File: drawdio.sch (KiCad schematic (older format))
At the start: 12 parts, among them P1 CONN_2, Q1 BC558, Q2 BC547, U1 LM555N

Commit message: Heavy work
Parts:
- removed P1: CONN_2, Pin_Headers:Pin_Header_Straight_1x02, symbol CONN_2
- removed P?: CONN_01X01, symbol CONN_01X01
- added P1: CONN_01X01, drawdio:Drawdio conn, symbol CONN_01X01
- added P2: CONN_01X02, drawdio:RS_mini_speaker_724-3100, symbol CONN_01X02
- added P3: CONN_01X01, drawdio:Drawdio_conn, symbol CONN_01X01
- added Q3: BC558, Housings_TO-92:TO-92_Molded_Wide_Oval, symbol BC558
- added Q4: BC547, Housings_TO-92:TO-92_Molded_Wide_Oval, symbol BC547
- BT1: footprint Pin_Headers:Pin_Header_Straight_1x02 -> drawdio:CR2025_Keystone_3002_button_cell_holder_SMT
- Q1, Q2: footprint drawdio:TO-92_JorFru_compact -> Housings_TO-92:TO-92_Molded_Wide_Oval
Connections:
- net GND: now also Q4.3 (E)
- net VCC: now also Q1.3 (E), Q3.3 (E); no longer Q1.1 (C)
- net at Q1.2 (B), Q2.2 (B): now also P2.2 (P2), Q3.1 (C), Q4.1 (C); no longer U1.3 (Q)
- net at R2.1, U1.7 (DIS): now also P3.1 (P1)
- net at R1.1: now also P1.1 (P1)
- net at C4.1, Q2.1 (C): now also Q1.1 (C); no longer Q1.3 (E)
- net at C4.2: now also P2.1 (P1)
- new net: Q3.2 (B), Q4.2 (B), U1.3 (Q)
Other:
- moved on the sheet: C4, Q1, Q2
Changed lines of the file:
@@
 LIBS:memory
 LIBS:xilinx
-LIBS:special
 LIBS:microcontrollers
 LIBS:dsp
@@
 $EndComp
 $Comp
-L CONN_2 P1
-U 1 1 5535819F
-P 5350 2000
-F 0 "P1" V 5300 2000 40  0000 C CNN
-F 1 "CONN_2" V 5400 2000 40  0000 C CNN
-F 2 "Pin_Headers:Pin_Header_Straight_1x02" H 5350 2000 60  0001 C CNN
-F 3 "" H 5350 2000 60  0000 C CNN
-	1    5350 2000
-	0    -1   -1   0
-$EndComp
-$Comp
 L R-RESCUE-drawdio R1
 U 1 1 55358209
@@
 L GND-RESCUE-drawdio #PWR01
 U 1 1 5535831F
-P 7400 4600
-F 0 "#PWR01" H 7400 4600 30  0001 C CNN
-F 1 "GND" H 7400 4530 30  0001 C CNN
-F 2 "" H 7400 4600 60  0000 C CNN
-F 3 "" H 7400 4600 60  0000 C CNN
-	1    7400 4600
+P 7950 4600
+F 0 "#PWR01" H 7950 4600 30  0001 C CNN
+F 1 "GND" H 7950 4530 30  0001 C CNN
+F 2 "" H 7950 4600 60  0000 C CNN
+F 3 "" H 7950 4600 60  0000 C CNN
+	1    7950 4600
 	1    0    0    -1
 $EndComp
@@
 $EndComp
 $Comp
-L BC547 Q2
-U 1 1 553583A7
-P 7300 4250
-F 0 "Q2" H 7300 4101 40  0000 R CNN
-F 1 "BC547" H 7300 4400 40  0000 R CNN
-F 2 "drawdio:TO-92_JorFru_compact" H 7200 4352 29  0000 C CNN
-F 3 "" H 7300 4250 60  0000 C CNN
-	1    7300 4250
-	1    0    0    -1
-$EndComp
-$Comp
 L BC558 Q1
 U 1 1 553583B6
-P 7300 3750
-F 0 "Q1" H 7300 3601 40  0000 R CNN
-F 1 "BC558" H 7300 3900 40  0000 R CNN
-F 2 "drawdio:TO-92_JorFru_compact" H 7200 3852 29  0000 C CNN
-F 3 "" H 7300 3750 60  0000 C CNN
-	1    7300 3750
-	1    0    0    -1
+P 7850 3750
+F 0 "Q1" H 7850 3601 40  0000 R CNN
+F 1 "BC558" H 7850 3900 40  0000 R CNN
+F 2 "Housings_TO-92:TO-92_Molded_Wide_Oval" H 7750 3852 29  0000 C CNN
+F 3 "" H 7850 3750 60  0000 C CNN
+	1    7850 3750
+	1    0    0    1
 $EndComp
 $Comp
 L CP-RESCUE-drawdio C4
 U 1 1 55358485
-P 7700 4000
-F 0 "C4" H 7750 4100 40  0000 L CNN
-F 1 "CP" H 7750 3900 40  0000 L CNN
-F 2 "Capacitors_Elko_ThroughHole:Elko_vert_11.2x6.3mm_RM2.5" H 7800 3850 30  0000 C CNN
-F 3 "~" H 7700 4000 300 0000 C CNN
-	1    7700 4000
-	0    -1   -1   0
+P 8450 4200
+F 0 "C4" H 8500 4300 40  0000 L CNN
+F 1 "CP" H 8500 4100 40  0000 L CNN
+F 2 "Capacitors_Elko_ThroughHole:Elko_vert_11.2x6.3mm_RM2.5" H 8550 4050 30  0000 C CNN
+F 3 "~" H 8450 4200 300 0000 C CNN
+	1    8450 4200
+	1    0    0    -1
 $EndComp
 $Comp
@@
 $EndComp
 $Comp
-L GND-RESCUE-drawdio #PWR06
+L GND-RESCUE-drawdio #PWR05
 U 1 1 553585E1
 P 3650 5050
-F 0 "#PWR06" H 3650 5050 30  0001 C CNN
+F 0 "#PWR05" H 3650 5050 30  0001 C CNN
 F 1 "GND" H 3650 4980 30  0001 C CNN
 F 2 "" H 3650 5050 60  0000 C CNN
@@
 $EndComp
 $Comp
-L VCC #PWR07
+L VCC #PWR06
 U 1 1 553585F0
-P 7400 3550
-F 0 "#PWR07" H 7400 3650 30  0001 C CNN
-F 1 "VCC" H 7400 3650 30  0000 C CNN
-F 2 "" H 7400 3550 60  0000 C CNN
-F 3 "" H 7400 3550 60  0000 C CNN
-	1    7400 3550
+P 7950 3550
+F 0 "#PWR06" H 7950 3650 30  0001 C CNN
+F 1 "VCC" H 7950 3650 30  0000 C CNN
+F 2 "" H 7950 3550 60  0000 C CNN
+F 3 "" H 7950 3550 60  0000 C CNN
+	1    7950 3550
 	1    0    0    -1
 $EndComp
@@
 F 0 "BT1" H 3250 4800 50  0000 C CNN
 F 1 "BATTERY" H 3250 4410 50  0000 C CNN
-F 2 "Pin_Headers:Pin_Header_Straight_1x02" H 3250 4600 60  0000 C CNN
+F 2 "drawdio:CR2025_Keystone_3002_button_cell_holder_SMT" H 3250 4600 60  0000 C CNN
 F 3 "~" H 3250 4600 60  0000 C CNN
 	1    3250 4600
@@
 $EndComp
 $Comp
-L GND-RESCUE-drawdio #PWR08
+L GND-RESCUE-drawdio #PWR07
 U 1 1 558086F5
 P 4600 4550
-F 0 "#PWR08" H 4600 4550 30  0001 C CNN
+F 0 "#PWR07" H 4600 4550 30  0001 C CNN
 F 1 "GND" H 4600 4480 30  0001 C CNN
 F 2 "" H 4600 4550 60  0000 C CNN
@@
 $EndComp
 $Comp
-L VCC #PWR09
+L VCC #PWR08
 U 1 1 55808C03
 P 3650 4250
-F 0 "#PWR09" H 3650 4350 30  0001 C CNN
+F 0 "#PWR08" H 3650 4350 30  0001 C CNN
 F 1 "VCC" H 3650 4350 30  0000 C CNN
 F 2 "" H 3650 4250 60  0000 C CNN
@@
 	6550 3950 6300 3950
 Wire Wire Line
-	7400 4600 7400 4450
+	7950 4600 7950 4450
 Wire Wire Line
 	4600 4000 4900 4000
@@
 Wire Wire Line
 	7150 2750 7050 2750
-Wire Wire Line
-	6300 3750 7100 3750
-Wire Wire Line
-	7400 3950 7400 4050
-Wire Wire Line
-	7050 3750 7050 4250
-Wire Wire Line
-	7050 4250 7100 4250
-Connection ~ 7050 3750
-Wire Wire Line
-	7400 4000 7500 4000
-Connection ~ 7400 4000
 Wire Wire Line
 	6550 5550 6550 5400
 Connection ~ 6550 4900
 Wire Wire Line
-	7900 4000 8200 4000
-Wire Wire Line
 	4650 2750 5250 2750
 Wire Wire Line
@@
 Wire Wire Line
 	4600 4550 4600 4400
-$Comp
-L CONN_01X01 P?
-U 1 1 55EF137E
-P 8400 4000
-F 0 "P?" H 8400 4100 50  0000 C CNN
-F 1 "CONN_01X01" V 8500 4000 50  0000 C CNN
-F 2 "" H 8400 4000 60  0000 C CNN
-F 3 "" H 8400 4000 60  0000 C CNN
-	1    8400 4000
-	1    0    0    -1
-$EndComp
-Connection ~ 8200 4000
-Connection ~ 7900 4000
-Connection ~ 7500 4000
+Connection ~ 8450 4800
+$Comp
+L CONN_01X01 P1
+U 1 1 56241D86
+P 5250 2150
+F 0 "P1" H 5250 2250 50  0000 C CNN
+F 1 "CONN_01X01" V 5350 2150 50  0000 C CNN
+F 2 "drawdio:Drawdio conn" H 5250 2150 60  0001 C CNN
+F 3 "" H 5250 2150 60  0000 C CNN
+	1    5250 2150
+	0    -1   -1   0
+$EndComp
+$Comp
+L CONN_01X01 P3
+U 1 1 56241E1F
+P 5450 2150
+F 0 "P3" H 5450 2250 50  0000 C CNN
+F 1 "CONN_01X01" V 5550 2150 50  0000 C CNN
+F 2 "drawdio:Drawdio_conn" H 5450 2150 60  0001 C CNN
+F 3 "" H 5450 2150 60  0000 C CNN
+	1    5450 2150
+	0    -1   -1   0
+$EndComp
+$Comp
+L BC547 Q2
+U 1 1 553583A7
+P 7850 4250
+F 0 "Q2" H 7850 4101 40  0000 R CNN
+F 1 "BC547" H 7850 4400 40  0000 R CNN
+F 2 "Housings_TO-92:TO-92_Molded_Wide_Oval" H 7750 4352 29  0000 C CNN
+F 3 "" H 7850 4250 60  0000 C CNN
+	1    7850 4250
+	1    0    0    -1
+$EndComp
+$Comp
+L GND-RESCUE-drawdio #PWR09
+U 1 1 56243975
+P 7400 4600
+F 0 "#PWR09" H 7400 4600 30  0001 C CNN
+F 1 "GND" H 7400 4530 30  0001 C CNN
+F 2 "" H 7400 4600 60  0000 C CNN
+F 3 "" H 7400 4600 60  0000 C CNN
+	1    7400 4600
+	1    0    0    -1
+$EndComp
+$Comp
+L BC558 Q3
+U 1 1 5624397B
+P 7300 3750
+F 0 "Q3" H 7300 3601 40  0000 R CNN
+F 1 "BC558" H 7300 3900 40  0000 R CNN
+F 2 "Housings_TO-92:TO-92_Molded_Wide_Oval" H 7200 3852 29  0000 C CNN
+F 3 "" H 7300 3750 60  0000 C CNN
+	1    7300 3750
+	1    0    0    1
+$EndComp
+$Comp
+L VCC #PWR010
+U 1 1 56243981
+P 7400 3550
+F 0 "#PWR010" H 7400 3650 30  0001 C CNN
+F 1 "VCC" H 7400 3650 30  0000 C CNN
+F 2 "" H 7400 3550 60  0000 C CNN
+F 3 "" H 7400 3550 60  0000 C CNN
+	1    7400 3550
+	1    0    0    -1
+$EndComp
+Wire Wire Line
+	7400 4600 7400 4450
+$Comp
+L BC547 Q4
+U 1 1 56243988
+P 7300 4250
+F 0 "Q4" H 7300 4101 40  0000 R CNN
+F 1 "BC547" H 7300 4400 40  0000 R CNN
+F 2 "Housings_TO-92:TO-92_Molded_Wide_Oval" H 7200 4352 29  0000 C CNN
+F 3 "" H 7300 4250 60  0000 C CNN
+	1    7300 4250
+	1    0    0    -1
+$EndComp
+Wire Wire Line
+	6300 3750 7100 3750
+Wire Wire Line
+	7100 3750 7100 4250
+Wire Wire Line
+	7400 3950 7400 4050
+Wire Wire Line
+	7400 4000 7650 4000
+Wire Wire Line
+	7650 3750 7650 4250
+Connection ~ 7400 4000
+Connection ~ 7650 4000
+Wire Wire Line
+	8450 4400 8450 4800
+Wire Wire Line
+	7950 3950 7950 4050
+Wire Wire Line
+	7950 4000 8450 4000
+Connection ~ 7950 4000
+Wire Wire Line
+	7550 4000 7550 4900
+Wire Wire Line
+	7550 4900 8450 4900
+Connection ~ 7550 4000
+$Comp
+L CONN_01X02 P2
+U 1 1 562400DE
+P 8650 4850
+F 0 "P2" H 8650 5000 50  0000 C CNN
+F 1 "CONN_01X02" V 8750 4850 50  0000 C CNN
+F 2 "drawdio:RS_mini_speaker_724-3100" H 8650 4850 60  0001 C CNN
+F 3 "" H 8650 4850 60  0000 C CNN
+	1    8650 4850
+	1    0    0    -1
+$EndComp
 $EndSCHEMATC

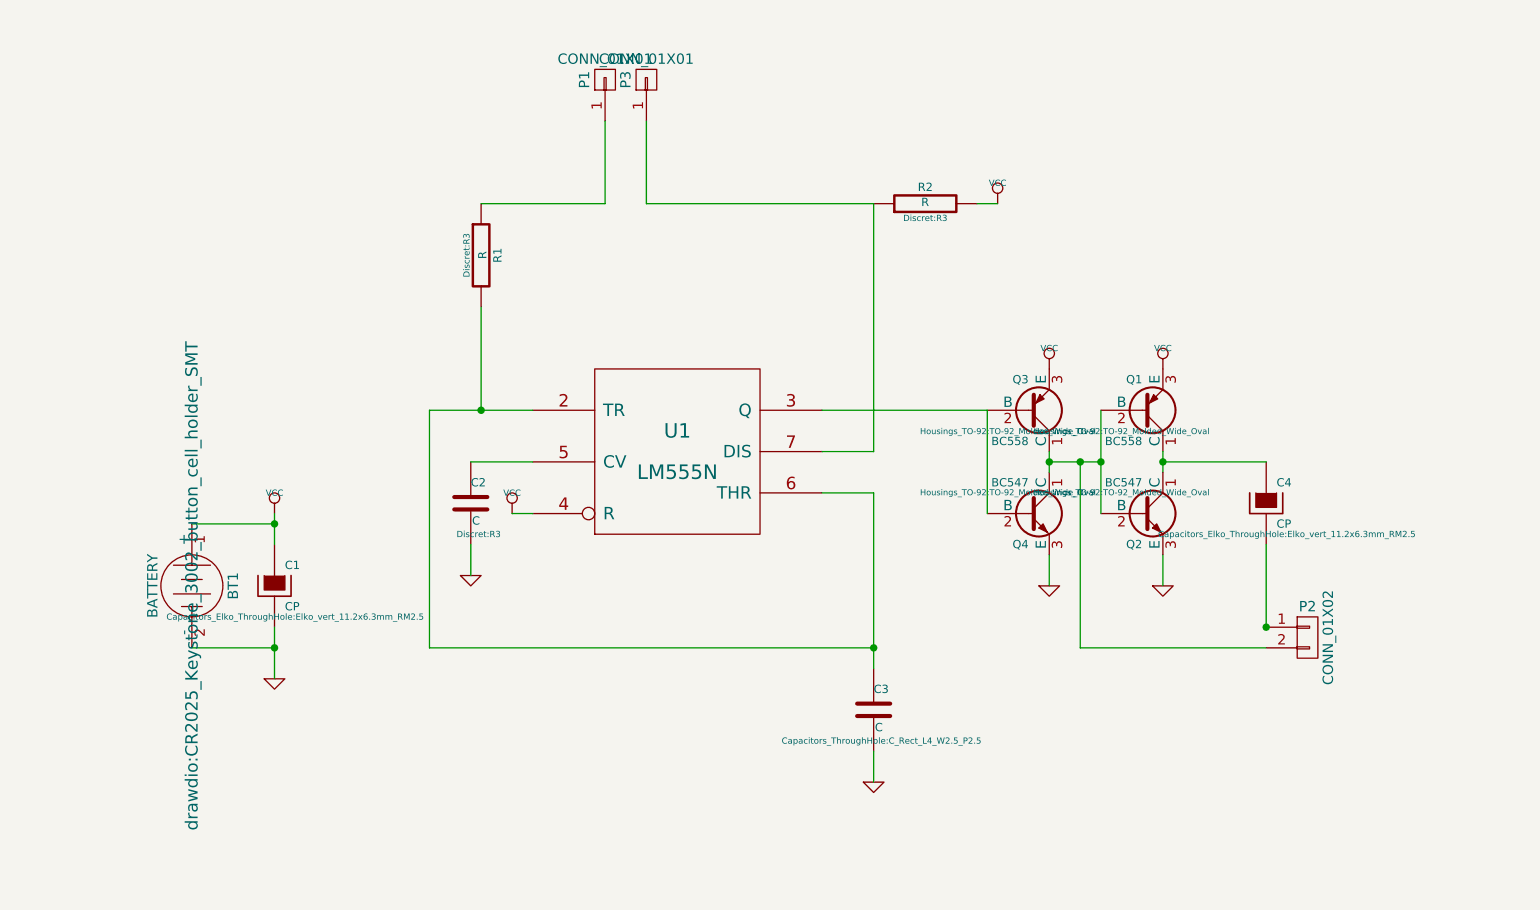
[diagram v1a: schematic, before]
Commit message: Added holes
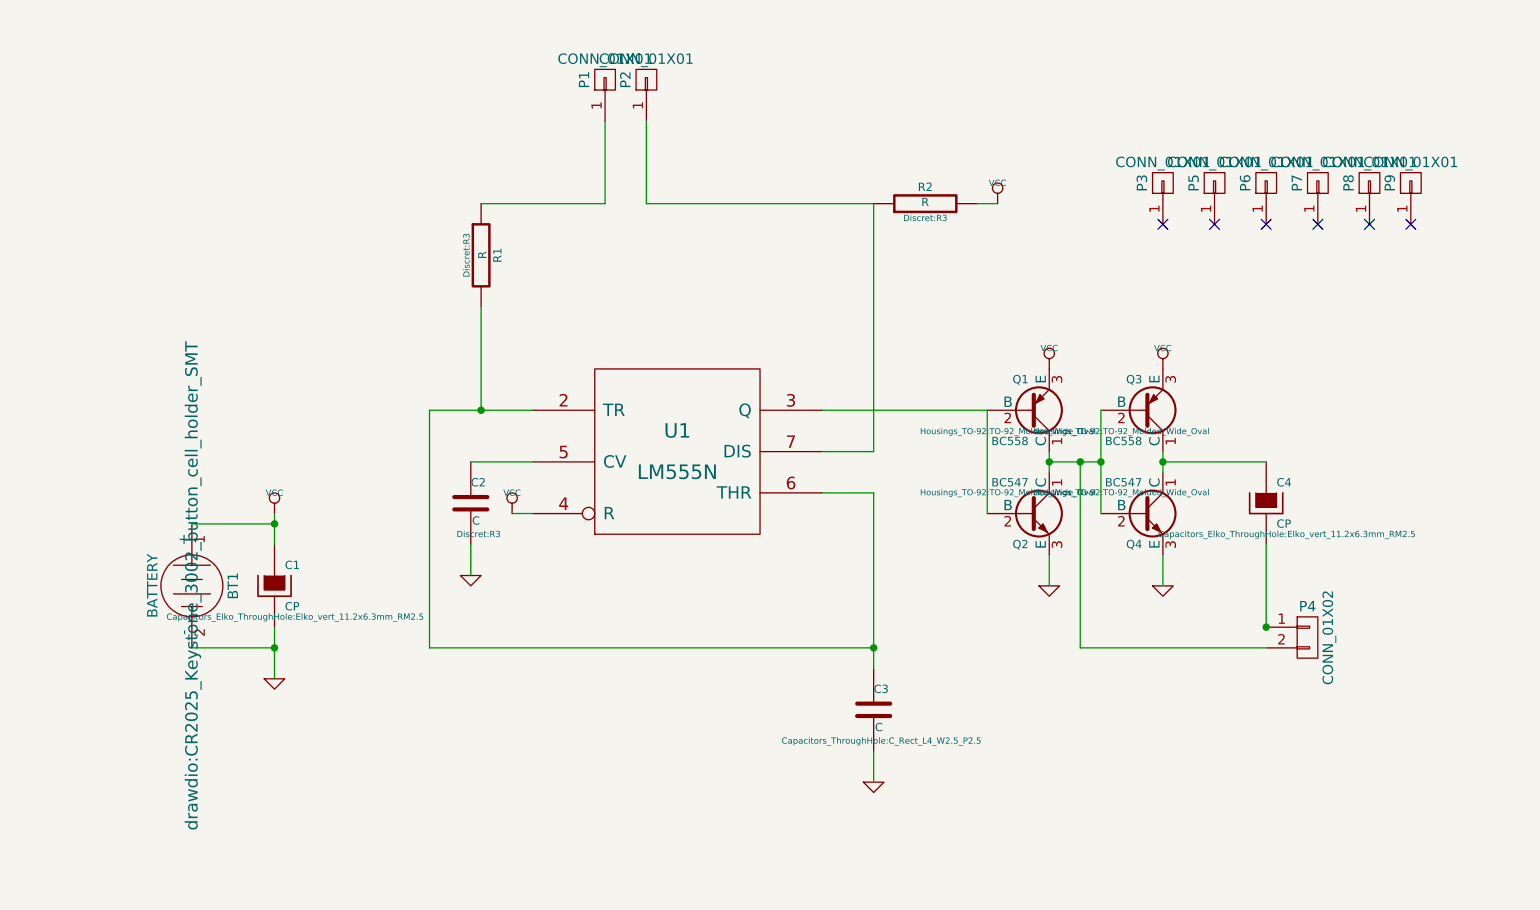
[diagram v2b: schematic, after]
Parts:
- added P3, P5, P6, P7: CONN_01X01, Mounting_Holes:MountingHole_2-5mm, symbol CONN_01X01
- added P8: CONN_01X01, drawdio:Symbol_OSHW-Logo_SilkScreen_BIG, symbol CONN_01X01
- added P9: CONN_01X01, symbol CONN_01X01
- P1: footprint drawdio:Drawdio conn -> drawdio:Drawdio_conn
- renumbered P3 to P2, P2 to P4, Q3 to Q1, Q4 to Q2, Q1 to Q3, Q2 to Q4
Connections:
- no-connect marks 0 -> 6
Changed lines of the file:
@@
 $EndComp
 $Comp
-L BC558 Q1
+L BC558 Q3
 U 1 1 553583B6
 P 7850 3750
-F 0 "Q1" H 7850 3601 40  0000 R CNN
+F 0 "Q3" H 7850 3601 40  0000 R CNN
 F 1 "BC558" H 7850 3900 40  0000 R CNN
 F 2 "Housings_TO-92:TO-92_Molded_Wide_Oval" H 7750 3852 29  0000 C CNN
@@
 F 0 "P1" H 5250 2250 50  0000 C CNN
 F 1 "CONN_01X01" V 5350 2150 50  0000 C CNN
-F 2 "drawdio:Drawdio conn" H 5250 2150 60  0001 C CNN
+F 2 "drawdio:Drawdio_conn" H 5250 2150 60  0001 C CNN
 F 3 "" H 5250 2150 60  0000 C CNN
 	1    5250 2150
@@
 $EndComp
 $Comp
-L CONN_01X01 P3
+L CONN_01X01 P2
 U 1 1 56241E1F
 P 5450 2150
-F 0 "P3" H 5450 2250 50  0000 C CNN
+F 0 "P2" H 5450 2250 50  0000 C CNN
 F 1 "CONN_01X01" V 5550 2150 50  0000 C CNN
 F 2 "drawdio:Drawdio_conn" H 5450 2150 60  0001 C CNN
@@
 $EndComp
 $Comp
-L BC547 Q2
+L BC547 Q4
 U 1 1 553583A7
 P 7850 4250
-F 0 "Q2" H 7850 4101 40  0000 R CNN
+F 0 "Q4" H 7850 4101 40  0000 R CNN
 F 1 "BC547" H 7850 4400 40  0000 R CNN
 F 2 "Housings_TO-92:TO-92_Molded_Wide_Oval" H 7750 4352 29  0000 C CNN
@@
 $EndComp
 $Comp
-L BC558 Q3
+L BC558 Q1
 U 1 1 5624397B
 P 7300 3750
-F 0 "Q3" H 7300 3601 40  0000 R CNN
+F 0 "Q1" H 7300 3601 40  0000 R CNN
 F 1 "BC558" H 7300 3900 40  0000 R CNN
 F 2 "Housings_TO-92:TO-92_Molded_Wide_Oval" H 7200 3852 29  0000 C CNN
@@
 	7400 4600 7400 4450
 $Comp
-L BC547 Q4
+L BC547 Q2
 U 1 1 56243988
 P 7300 4250
-F 0 "Q4" H 7300 4101 40  0000 R CNN
+F 0 "Q2" H 7300 4101 40  0000 R CNN
 F 1 "BC547" H 7300 4400 40  0000 R CNN
 F 2 "Housings_TO-92:TO-92_Molded_Wide_Oval" H 7200 4352 29  0000 C CNN
@@
 Connection ~ 7550 4000
 $Comp
-L CONN_01X02 P2
+L CONN_01X02 P4
 U 1 1 562400DE
 P 8650 4850
-F 0 "P2" H 8650 5000 50  0000 C CNN
+F 0 "P4" H 8650 5000 50  0000 C CNN
 F 1 "CONN_01X02" V 8750 4850 50  0000 C CNN
 F 2 "drawdio:RS_mini_speaker_724-3100" H 8650 4850 60  0001 C CNN
@@
 	1    0    0    -1
 $EndComp
+$Comp
+L CONN_01X01 P3
+U 1 1 56249E74
+P 7950 2650
+F 0 "P3" H 7950 2750 50  0000 C CNN
+F 1 "CONN_01X01" V 8050 2650 50  0000 C CNN
+F 2 "Mounting_Holes:MountingHole_2-5mm" H 7950 2650 60  0001 C CNN
+F 3 "" H 7950 2650 60  0000 C CNN
+	1    7950 2650
+	0    -1   -1   0
+$EndComp
+$Comp
+L CONN_01X01 P5
+U 1 1 56249F93
+P 8200 2650
+F 0 "P5" H 8200 2750 50  0000 C CNN
+F 1 "CONN_01X01" V 8300 2650 50  0000 C CNN
+F 2 "Mounting_Holes:MountingHole_2-5mm" H 8200 2650 60  0001 C CNN
+F 3 "" H 8200 2650 60  0000 C CNN
+	1    8200 2650
+	0    -1   -1   0
+$EndComp
+$Comp
+L CONN_01X01 P6
+U 1 1 56249FEB
+P 8450 2650
+F 0 "P6" H 8450 2750 50  0000 C CNN
+F 1 "CONN_01X01" V 8550 2650 50  0000 C CNN
+F 2 "Mounting_Holes:MountingHole_2-5mm" H 8450 2650 60  0001 C CNN
+F 3 "" H 8450 2650 60  0000 C CNN
+	1    8450 2650
+	0    -1   -1   0
+$EndComp
+$Comp
+L CONN_01X01 P7
+U 1 1 5624A048
+P 8700 2650
+F 0 "P7" H 8700 2750 50  0000 C CNN
+F 1 "CONN_01X01" V 8800 2650 50  0000 C CNN
+F 2 "Mounting_Holes:MountingHole_2-5mm" H 8700 2650 60  0001 C CNN
+F 3 "" H 8700 2650 60  0000 C CNN
+	1    8700 2650
+	0    -1   -1   0
+$EndComp
+NoConn ~ 7950 2850
+NoConn ~ 8200 2850
+NoConn ~ 8450 2850
+NoConn ~ 8700 2850
+$Comp
+L CONN_01X01 P8
+U 1 1 5624AD30
+P 8950 2650
+F 0 "P8" H 8950 2750 50  0000 C CNN
+F 1 "CONN_01X01" V 9050 2650 50  0000 C CNN
+F 2 "drawdio:Symbol_OSHW-Logo_SilkScreen_BIG" H 8950 2650 60  0001 C CNN
+F 3 "" H 8950 2650 60  0000 C CNN
+	1    8950 2650
+	0    -1   -1   0
+$EndComp
+NoConn ~ 8950 2850
+NoConn ~ 9150 2850
+$Comp
+L CONN_01X01 P9
+U 1 1 5624B4CA
+P 9150 2650
+F 0 "P9" H 9150 2750 50  0000 C CNN
+F 1 "CONN_01X01" V 9250 2650 50  0000 C CNN
+F 2 "" H 9150 2650 60  0000 C CNN
+F 3 "" H 9150 2650 60  0000 C CNN
+	1    9150 2650
+	0    -1   -1   0
+$EndComp
 $EndSCHEMATC

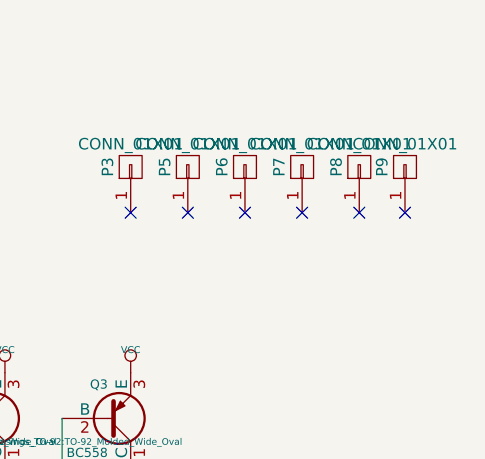
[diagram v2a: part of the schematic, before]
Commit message: Added holes
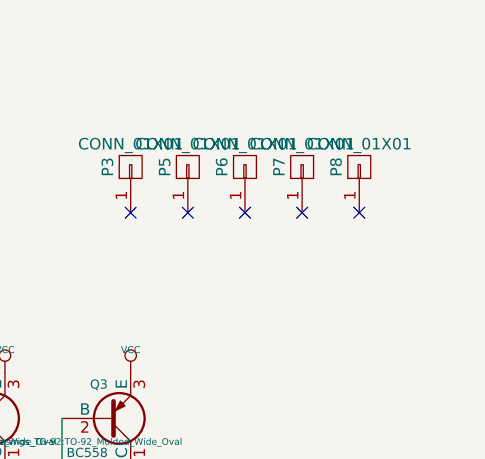
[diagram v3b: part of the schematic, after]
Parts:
- removed P9: CONN_01X01, symbol CONN_01X01
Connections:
- no-connect marks 6 -> 5
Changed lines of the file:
@@
 $EndComp
 NoConn ~ 8950 2850
-NoConn ~ 9150 2850
-$Comp
-L CONN_01X01 P9
-U 1 1 5624B4CA
-P 9150 2650
-F 0 "P9" H 9150 2750 50  0000 C CNN
-F 1 "CONN_01X01" V 9250 2650 50  0000 C CNN
-F 2 "" H 9150 2650 60  0000 C CNN
-F 3 "" H 9150 2650 60  0000 C CNN
-	1    9150 2650
-	0    -1   -1   0
-$EndComp
 $EndSCHEMATC
